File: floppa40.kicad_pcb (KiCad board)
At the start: 2 copper layers, 20 parts

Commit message: real
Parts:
- removed the REF** at (99.0, 63.8)
- removed the REF** at (108.0, 46.8)
- removed the REF** at (49.5, 29.8)
- removed the REF** at (72.0, 80.8)
- removed the REF** at (81.0, 63.8)
- removed the REF** at (90.0, 46.8)
- removed the REF** at (54.0, 46.8)
- removed the REF** at (126.0, 46.8)
- removed the REF** at (103.5, 29.8)
- removed the REF** at (63.0, 63.8)
- removed the REF** at (38.2, 63.8)
- removed the REF** at (121.5, 29.8)
- removed the REF** at (31.5, 29.8)
- removed the REF** at (72.0, 46.8)
- removed the REF** at (33.8, 80.8)
- removed the REF** at (67.5, 29.8)
- removed the REF** at (33.8, 46.8)
- removed the REF** at (85.5, 29.8)
- removed the REF** at (54.0, 80.8)
- removed the REF** at (117.0, 63.8)
- added ': SW_Hotswap_Kailh_Choc_V1V2_1.25u, kailh:SW_Hotswap_Kailh_Choc_V1V2_1.25u, F.Cu at (236.2, 108.4)
- added ,: SW_Hotswap_Kailh_Choc_V1V2_1.00u, kailh:SW_Hotswap_Kailh_Choc_V1V2_1.00u, F.Cu at (202.5, 125.4)
- added .: SW_Hotswap_Kailh_Choc_V1V2_1.00u, kailh:SW_Hotswap_Kailh_Choc_V1V2_1.00u, F.Cu at (220.5, 125.4)
- added /: SW_Hotswap_Kailh_Choc_V1V2_1.25u, kailh:SW_Hotswap_Kailh_Choc_V1V2_1.25u, F.Cu at (258.8, 108.4)
- added ;: SW_Hotswap_Kailh_Choc_V1V2_1.00u, kailh:SW_Hotswap_Kailh_Choc_V1V2_1.00u, F.Cu at (216.0, 108.4)
- added J1: MJ-4PP-9, 42keebs-kicad:PJ-320A, F.Cu at (126.0, 51.0)
- added REF**: Right, 42keebs-kicad:PinHeader_2x13+5_P2.54mm_Vertical_Elite-C, F.Cu at (24.8, 55.2)
- added \: SW_Hotswap_Kailh_Choc_V1V2_1.00u, kailh:SW_Hotswap_Kailh_Choc_V1V2_1.00u, F.Cu at (238.5, 125.4)
- added a: SW_Hotswap_Kailh_Choc_V1V2_1.00u, kailh:SW_Hotswap_Kailh_Choc_V1V2_1.00u, F.Cu at (54.0, 91.4)
- added alt: SW_Hotswap_Kailh_Choc_V1V2_1.25u, kailh:SW_Hotswap_Kailh_Choc_V1V2_1.25u, F.Cu at (78.8, 125.4)
- added b: SW_Hotswap_Kailh_Choc_V1V2_1.00u, kailh:SW_Hotswap_Kailh_Choc_V1V2_1.00u, F.Cu at (162.0, 108.4)
- added backspace: SW_Hotswap_Kailh_Choc_V1V2_1.25u, kailh:SW_Hotswap_Kailh_Choc_V1V2_1.25u, F.Cu at (258.8, 74.4)
- added c: SW_Hotswap_Kailh_Choc_V1V2_1.00u, kailh:SW_Hotswap_Kailh_Choc_V1V2_1.00u, F.Cu at (99.0, 108.4)
- added ctrl: SW_Hotswap_Kailh_Choc_V1V2_1.25u, kailh:SW_Hotswap_Kailh_Choc_V1V2_1.25u, F.Cu at (33.8, 125.4)
- added d: SW_Hotswap_Kailh_Choc_V1V2_1.00u, kailh:SW_Hotswap_Kailh_Choc_V1V2_1.00u, F.Cu at (90.0, 91.4)
- added e: SW_Hotswap_Kailh_Choc_V1V2_1.00u, kailh:SW_Hotswap_Kailh_Choc_V1V2_1.00u, F.Cu at (85.5, 74.4)
- added enter: SW_Hotswap_Kailh_Choc_V1V2_2.00u, kailh:SW_Hotswap_Kailh_Choc_V1V2_2.00u, F.Cu at (252.0, 91.4)
- added esc: SW_Hotswap_Kailh_Choc_V1V2_1.00u, kailh:SW_Hotswap_Kailh_Choc_V1V2_1.00u, F.Cu at (31.5, 74.4)
- added f: SW_Hotswap_Kailh_Choc_V1V2_1.00u, kailh:SW_Hotswap_Kailh_Choc_V1V2_1.00u, F.Cu at (108.0, 91.4)
- added g: SW_Hotswap_Kailh_Choc_V1V2_1.00u, kailh:SW_Hotswap_Kailh_Choc_V1V2_1.00u, F.Cu at (126.0, 91.4)
- added h: SW_Hotswap_Kailh_Choc_V1V2_1.00u, kailh:SW_Hotswap_Kailh_Choc_V1V2_1.00u, F.Cu at (171.0, 91.4)
- added i: SW_Hotswap_Kailh_Choc_V1V2_1.00u, kailh:SW_Hotswap_Kailh_Choc_V1V2_1.00u, F.Cu at (202.5, 74.4)
- added j: SW_Hotswap_Kailh_Choc_V1V2_1.00u, kailh:SW_Hotswap_Kailh_Choc_V1V2_1.00u, F.Cu at (189.0, 91.4)
- added k: SW_Hotswap_Kailh_Choc_V1V2_1.00u, kailh:SW_Hotswap_Kailh_Choc_V1V2_1.00u, F.Cu at (207.0, 91.4)
- added l: SW_Hotswap_Kailh_Choc_V1V2_1.00u, kailh:SW_Hotswap_Kailh_Choc_V1V2_1.00u, F.Cu at (225.0, 91.4)
- added m: SW_Hotswap_Kailh_Choc_V1V2_1.00u, kailh:SW_Hotswap_Kailh_Choc_V1V2_1.00u, F.Cu at (198.0, 108.4)
- added mod: SW_Hotswap_Kailh_Choc_V1V2_1.25u, kailh:SW_Hotswap_Kailh_Choc_V1V2_1.25u, F.Cu at (258.8, 125.4)
- added n: SW_Hotswap_Kailh_Choc_V1V2_1.00u, kailh:SW_Hotswap_Kailh_Choc_V1V2_1.00u, F.Cu at (180.0, 108.4)
- added o: SW_Hotswap_Kailh_Choc_V1V2_1.00u, kailh:SW_Hotswap_Kailh_Choc_V1V2_1.00u, F.Cu at (220.5, 74.4)
- added p: SW_Hotswap_Kailh_Choc_V1V2_1.00u, kailh:SW_Hotswap_Kailh_Choc_V1V2_1.00u, F.Cu at (238.5, 74.4)
- added q: SW_Hotswap_Kailh_Choc_V1V2_1.00u, kailh:SW_Hotswap_Kailh_Choc_V1V2_1.00u, F.Cu at (49.5, 74.4)
- added r: SW_Hotswap_Kailh_Choc_V1V2_1.00u, kailh:SW_Hotswap_Kailh_Choc_V1V2_1.00u, F.Cu at (103.5, 74.4)
- added s: SW_Hotswap_Kailh_Choc_V1V2_1.00u, kailh:SW_Hotswap_Kailh_Choc_V1V2_1.00u, F.Cu at (72.0, 91.4)
- added shift: SW_Hotswap_Kailh_Choc_V1V2_1.75u, kailh:SW_Hotswap_Kailh_Choc_V1V2_1.75u, F.Cu at (38.2, 108.4)
- added space: SW_Hotswap_Kailh_Choc_V1V2_2.00u, kailh:SW_Hotswap_Kailh_Choc_V1V2_2.00u, F.Cu at (175.5, 125.4)
- added space: SW_Hotswap_Kailh_Choc_V1V2_2.25u, kailh:SW_Hotswap_Kailh_Choc_V1V2_2.25u, F.Cu at (110.2, 125.4)
- added super: SW_Hotswap_Kailh_Choc_V1V2_1.25u, kailh:SW_Hotswap_Kailh_Choc_V1V2_1.25u, F.Cu at (56.2, 125.4)
- added t: SW_Hotswap_Kailh_Choc_V1V2_1.00u, kailh:SW_Hotswap_Kailh_Choc_V1V2_1.00u, F.Cu at (121.5, 74.4)
- added tab: SW_Hotswap_Kailh_Choc_V1V2_1.25u, kailh:SW_Hotswap_Kailh_Choc_V1V2_1.25u, F.Cu at (33.8, 91.4)
- added u: SW_Hotswap_Kailh_Choc_V1V2_1.00u, kailh:SW_Hotswap_Kailh_Choc_V1V2_1.00u, F.Cu at (184.5, 74.4)
- added v: SW_Hotswap_Kailh_Choc_V1V2_1.00u, kailh:SW_Hotswap_Kailh_Choc_V1V2_1.00u, F.Cu at (117.0, 108.4)
- added w: SW_Hotswap_Kailh_Choc_V1V2_1.00u, kailh:SW_Hotswap_Kailh_Choc_V1V2_1.00u, F.Cu at (67.5, 74.4)
- added x: SW_Hotswap_Kailh_Choc_V1V2_1.00u, kailh:SW_Hotswap_Kailh_Choc_V1V2_1.00u, F.Cu at (81.0, 108.4)
- added y: SW_Hotswap_Kailh_Choc_V1V2_1.00u, kailh:SW_Hotswap_Kailh_Choc_V1V2_1.00u, F.Cu at (166.5, 74.4)
- added z: SW_Hotswap_Kailh_Choc_V1V2_1.00u, kailh:SW_Hotswap_Kailh_Choc_V1V2_1.00u, F.Cu at (63.0, 108.4)
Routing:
- net (no net): track 0.00 -> 95.5 mm

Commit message: :)
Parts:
- removed the , at (202.5, 125.4)
- removed the . at (220.5, 125.4)
- removed \: SW_Hotswap_Kailh_Choc_V1V2_1.00u, kailh:SW_Hotswap_Kailh_Choc_V1V2_1.00u
- removed the mod at (258.8, 125.4)
- removed the space at (175.5, 125.4)
- added J1: MJ-4PP-9, 42keebs-kicad:PJ-320A, F.Cu at (164.1, 45.0)
- added OLED1: OLED, 42keebs-kicad:OLED_v2.1, F.Cu at (231.4, 54.5)
- added frood: Right, 42keebs-kicad:PinHeader_2x13+5_P2.54mm_Vertical_Elite-C, F.Cu at (171.1, 54.9)
- added mod: SW_Hotswap_Kailh_Choc_V1V2_1.50u, kailh:SW_Hotswap_Kailh_Choc_V1V2_1.50u, F.Cu at (257.6, 125.4)
- added space: SW_Hotswap_Kailh_Choc_V1V2_2.25u, kailh:SW_Hotswap_Kailh_Choc_V1V2_2.25u, F.Cu at (178.9, 125.4)
- moved J1 6.37 mm to (128.0, 45.0)
- moved , 1.12 mm to (217.1, 108.4)
- moved . 1.12 mm to (237.4, 108.4)
- moved / 1.12 mm to (259.9, 108.4)
- moved b 1.12 mm to (163.1, 108.4)
- moved backspace 1.12 mm to (259.9, 74.4)
- moved enter 1.12 mm to (253.1, 91.4)
- moved h 1.12 mm to (172.1, 91.4)
- moved i 1.12 mm to (203.6, 74.4)
- moved j 1.12 mm to (190.1, 91.4)
- moved k 1.12 mm to (208.1, 91.4)
- moved l 1.12 mm to (226.1, 91.4)
- moved m 1.12 mm to (199.1, 108.4)
- moved n 1.12 mm to (181.1, 108.4)
- moved o 1.12 mm to (221.6, 74.4)
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- renumbered ; to ,, ' to ., REF** to frood
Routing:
- net (no net): track 95.5 -> 790.0 mm
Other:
- board outline added: 248.6 x 90.3 mm

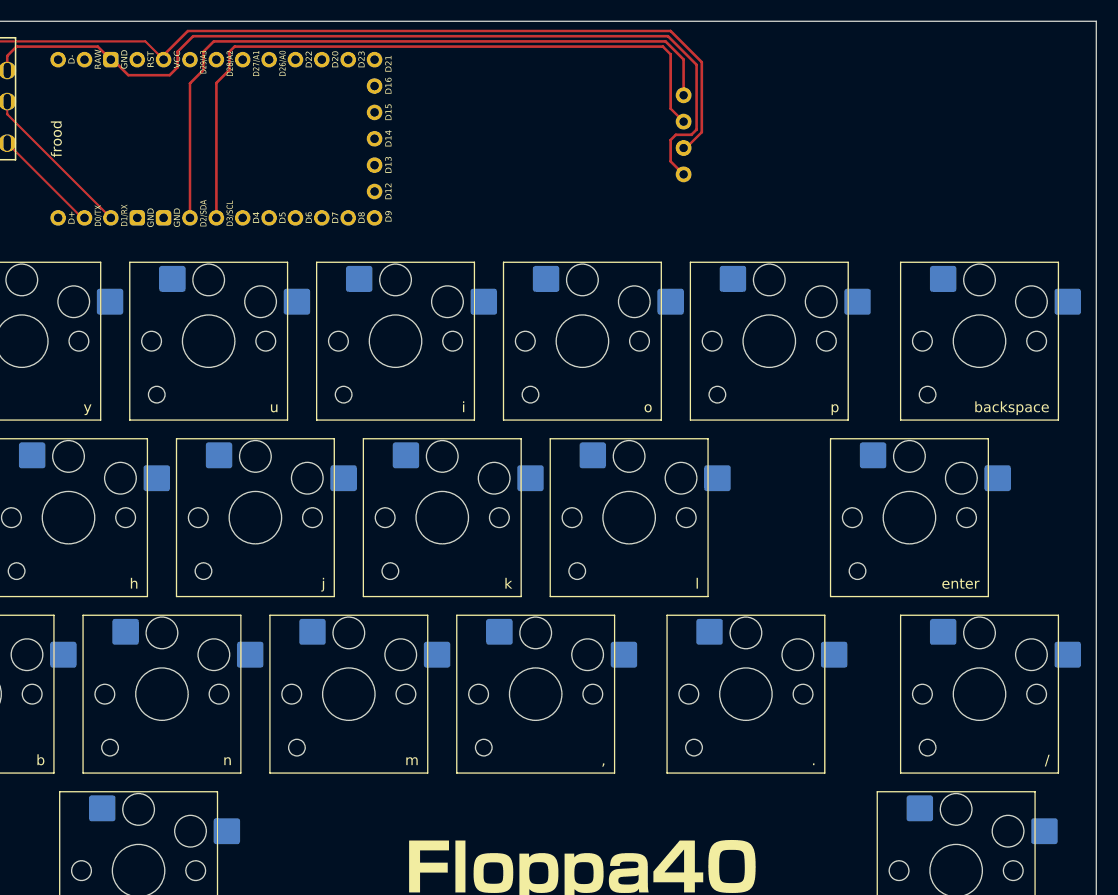
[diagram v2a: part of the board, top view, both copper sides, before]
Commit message: routed right side
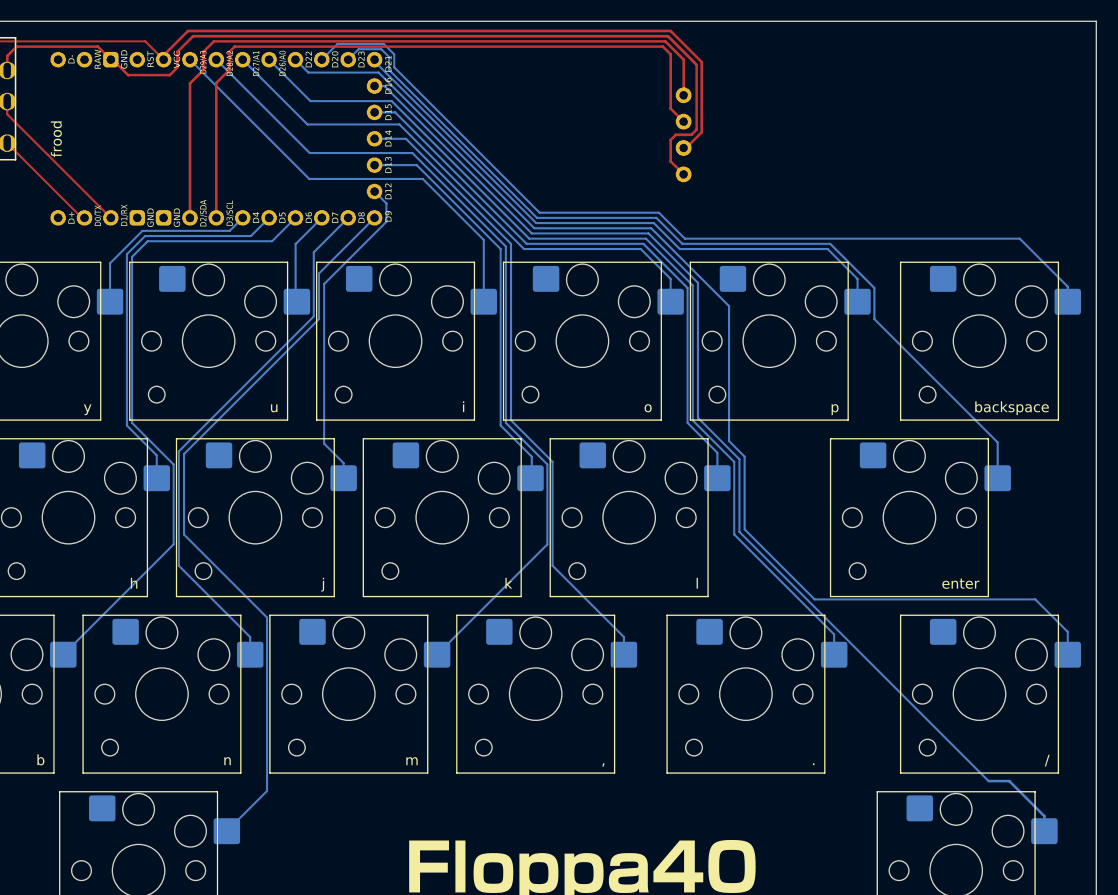
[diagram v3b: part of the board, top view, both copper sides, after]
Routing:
- net (no net): track 790.0 -> 1938.4 mm

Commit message: real
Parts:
- moved J1 3.53 mm to (162.0, 47.8)
- moved J1 3.47 mm to (126.0, 47.8)
- moved OLED1 2.02 mm to (229.5, 55.2)
- moved , 1.12 mm to (216.0, 108.4)
- moved . 1.12 mm to (236.2, 108.4)
- moved / 1.12 mm to (258.8, 108.4)
- moved b 1.12 mm to (162.0, 108.4)
- moved backspace 1.12 mm to (258.8, 74.4)
- moved enter 1.12 mm to (252.0, 91.4)
- moved h 1.12 mm to (171.0, 91.4)
- moved i 1.12 mm to (202.5, 74.4)
- moved j 1.12 mm to (189.0, 91.4)
- moved k 1.12 mm to (207.0, 91.4)
- moved l 1.12 mm to (225.0, 91.4)
- moved m 1.12 mm to (198.0, 108.4)
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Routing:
- net (no net): track 1938.4 -> 2088.1 mm
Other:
- board outline removed

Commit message: fart rounding edge cuts
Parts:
- moved frood 1.13 mm to (24.0, 54.9)
- moved a 1.13 mm to (52.9, 91.1)
- moved alt 1.13 mm to (77.7, 125.1)
- moved c 1.13 mm to (97.9, 108.1)
- moved ctrl 1.13 mm to (32.7, 125.1)
- moved d 1.13 mm to (88.9, 91.1)
- moved e 1.13 mm to (84.4, 74.1)
- moved esc 1.13 mm to (30.4, 74.1)
- moved f 1.13 mm to (106.9, 91.1)
- moved g 1.13 mm to (124.9, 91.1)
- moved q 1.13 mm to (48.4, 74.1)
- moved r 1.13 mm to (102.4, 74.1)
- moved s 1.13 mm to (70.9, 91.1)
- moved shift 1.13 mm to (37.2, 108.1)
- moved space 1.13 mm to (109.2, 125.1)
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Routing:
- net (no net): track 2088.1 -> 2084.7 mm
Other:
- board outline added: 248.6 x 89.2 mm

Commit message: :(
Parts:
- moved frood 1.13 mm to (25.1, 55.1)
- moved a 1.13 mm to (54.0, 91.4)
- moved alt 1.13 mm to (78.8, 125.4)
- moved c 1.13 mm to (99.0, 108.4)
- moved ctrl 1.13 mm to (33.8, 125.4)
- moved d 1.13 mm to (90.0, 91.4)
- moved e 1.13 mm to (85.5, 74.4)
- moved esc 1.13 mm to (31.5, 74.4)
- moved f 1.13 mm to (108.0, 91.4)
- moved g 1.13 mm to (126.0, 91.4)
- moved q 1.13 mm to (49.5, 74.4)
- moved r 1.13 mm to (103.5, 74.4)
- moved s 1.13 mm to (72.0, 91.4)
- moved shift 1.13 mm to (38.2, 108.4)
- moved space 1.13 mm to (110.2, 125.4)
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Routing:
- net (no net): track 2084.7 -> 3236.8 mm
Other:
- board size 248.6 x 89.2 mm -> 247.5 x 89.2 mm

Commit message: real
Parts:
- added ?: LOGO, floppa40:floppa, F.Cu at (67.5, 70.1)
- moved , 14.9 mm to (216.0, 123.2)
- moved . 14.9 mm to (236.2, 123.2)
- moved / 14.9 mm to (258.8, 123.2)
- moved J1 14.9 mm to (162.0, 62.7)
- moved J1 14.9 mm to (126.0, 62.6)
- moved OLED1 14.9 mm to (229.5, 70.1)
- moved a 14.9 mm to (54.0, 106.2)
- moved alt 14.9 mm to (78.8, 140.2)
- moved b 14.9 mm to (162.0, 123.2)
- moved backspace 14.9 mm to (258.8, 89.2)
- moved c 14.9 mm to (99.0, 123.2)
- moved ctrl 14.9 mm to (33.8, 140.2)
- moved d 14.9 mm to (90.0, 106.2)
- moved e 14.9 mm to (85.5, 89.2)
- moved enter 14.9 mm to (252.0, 106.2)
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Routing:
- net (no net): track 3236.8 -> 4307.9 mm, vias 0 -> 40
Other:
- outline, holes or cut-outs redrawn
